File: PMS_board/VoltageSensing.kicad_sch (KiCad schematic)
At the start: 66 parts, among them J2 BAT_SENSE1, J3 BAT_SENSE2, U1 LM324DR, U2 LM324DR

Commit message: Voltage Sensing and Capacitor Assign
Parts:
- removed R7: 54.9k, Resistor_SMD:R_0603_1608Metric_Pad0.98x0.95mm_HandSolder, symbol Device:R_US
- removed TP1, TP4, TP5: TestPoint, TestPoint:TestPoint_Pad_D1.0mm, symbol Connector:TestPoint
- added D15, D22, D30, D31, D32, D33: BZV55B3V3, Diode_SMD:D_MiniMELF, symbol Diode:BZV55B3V3
- added R101, R102: 54.9k, Resistor_SMD:R_0603_1608Metric_Pad0.98x0.95mm_HandSolder, symbol Device:R_US
- added R103, R104, R105, R106, R107, R108, R109, R110, R111, R112, R113, R114: 39.2k, Resistor_SMD:R_0603_1608Metric_Pad0.98x0.95mm_HandSolder, symbol Device:R_US
- added R115, R116, R117, R118, R119, R120: 1k, Resistor_SMD:R_0603_1608Metric_Pad0.98x0.95mm_HandSolder, symbol Device:R_US
- added TP25, TP26, TP27: TestPoint, TestPoint:TestPoint_Pad_D1.0mm, symbol Connector:TestPoint
- added U15, U3: LM324DR, Package_SO:SOIC-14_3.9x8.7mm_P1.27mm, symbol Amplifier_Operational:Opamp_Quad
- added U19: TS3A27518EIPWRQ1, PW24, symbol Symbols:TS3A27518EIPWRQ1
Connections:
- net +24V: now also U15.4 (V+), U3.4 (V+)
- net BATT1_CELL1: now also R17.2, TP21.1
- net BATT1_CELL2: now also R15.2
- net BATT1_CELL3: now also R13.2
- net BATT1_CELL4: now also R11.2; no longer TP3.1
- net BATT1_CELL5: now also R9.2, TP3.1
- net BATT1_CELL6: now also TP20.1, R101.1
- net BATT2_CELL1: no longer R17.1, TP24.1
- net BATT2_CELL2: no longer R15.1, TP23.1
- net BATT2_CELL3: no longer R13.1, TP22.1
- net BATT2_CELL4: no longer R11.1, TP21.1
- net BATT2_CELL5: no longer R9.1, TP20.1
- net GND: now also D15.2 (A), D22.2 (A), D30.2 (A), D31.2 (A), D32.2 (A), D33.2 (A), R102.2, R103.1, R105.1, R107.1, R109.1, R111.1, R113.1, U15.11 (V-), U19.20 (*EN), U19.5 (GND), U3.11 (V-)
- net VSENSE1: now also U19.4 (COM1); no longer D8.1 (K), R36.2, TP12.1
- net VSENSE2: now also U19.6 (COM2); no longer D7.1 (K), R35.2, TP11.1
- net VSENSE3: now also U19.7 (COM3); no longer D6.1 (K), R34.2, TP10.1
- net VSENSE4: now also U19.9 (COM4); no longer D5.1 (K), R33.2, TP9.1
- net VSENSE5: now also U19.10 (COM5); no longer D4.1 (K), R31.2, TP8.1
- net VSENSE6: now also U19.12 (COM6); no longer D3.1 (K), R32.2, TP7.1
- net at R14.1, R26.1, R27.2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: no longer R15.2
- net at R10.1, R22.1, R23.2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: no longer R11.2
- net at R20.1, R21.2, R8.1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: no longer R9.2
- net at R12.1, R24.1, R25.2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: no longer R13.2
- net at R16.1, R28.1, R29.2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: no longer R17.2
- new net: R108.1, R109.2, R13.1, U15.13 (-), U3.10 (+)
- new net: R106.2, R115.1, U3.14
- new net: R112.2, R119.1, U15.1
- new net: R112.1, R113.2, R17.1, U15.2 (-), U3.5 (+)
- new net: R110.1, R111.2, R15.1, U15.3 (+), U3.9 (-)
- new net: R104.1, R105.2, R9.1, U3.12 (+), U3.2 (-)
- new net: R106.1, R107.2, R11.1, U15.12 (+), U3.13 (-)
- new net: R108.2, R117.1, U15.14
- new net: R110.2, R118.1, U3.8
- new net: R102.1, R114.1, U3.6 (-)
- new net: R114.2, R120.1, U3.7
- new net: R104.2, R116.1, U3.1
- new net: R101.2, R103.2, U3.3 (+)
- new net +3.3V: U19.8 (V+)
- new net BATT1_SENS1: D8.1 (K), R36.2, TP12.1, U19.2 (NC1)
- new net BATT1_SENS2: D7.1 (K), R35.2, TP11.1, U19.1 (NC2)
- new net BATT1_SENS3: D6.1 (K), R34.2, TP10.1, U19.23 (NC3)
- new net BATT1_SENS4: D5.1 (K), R33.2, TP9.1, U19.21 (NC4)
- new net BATT1_SENS5: D4.1 (K), R31.2, TP8.1, U19.19 (NC5)
- new net BATT1_SENS6: D3.1 (K), R32.2, TP7.1, U19.22 (NC6)
- new net BATT2_SENS1: D33.1 (K), R120.2, TP27.1, U19.11 (NO1)
- new net BATT2_SENS2: D32.1 (K), R119.2, TP26.1, U19.13 (NO2)
- new net BATT2_SENS3: D31.1 (K), R118.2, TP25.1, U19.15 (NO3)
- new net BATT2_SENS4: D30.1 (K), R117.2, TP24.1, U19.17 (NO4)
- new net BATT2_SENS5: D22.1 (K), R115.2, TP23.1, U19.18 (NO5)
- new net BATT2_SENS6: D15.1 (K), R116.2, TP22.1, U19.16 (NO6)
- new net SW1: U19.24 (IN1)
- new net SW2: U19.14 (IN2)
- no-connect marks 2 -> 3
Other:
- moved on the sheet: D3, D4, D5, D6, D7, D8, D9, J2, J3, R10, R100, R12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

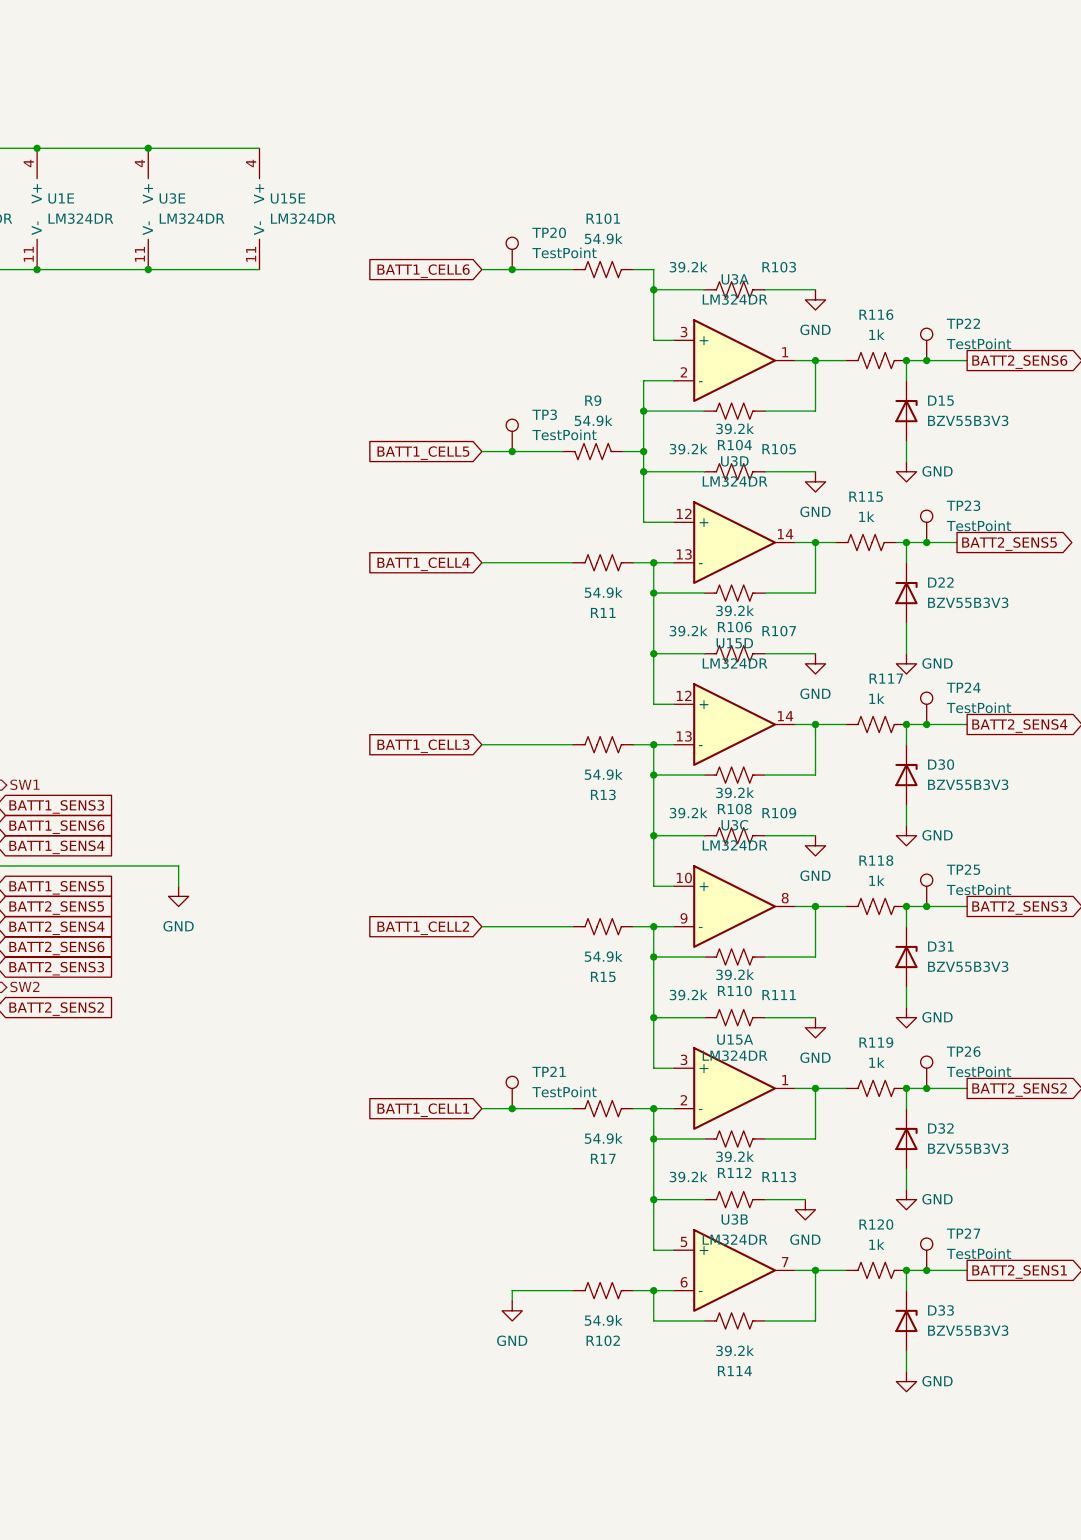
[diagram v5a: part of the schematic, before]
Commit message: Set some things to DNP
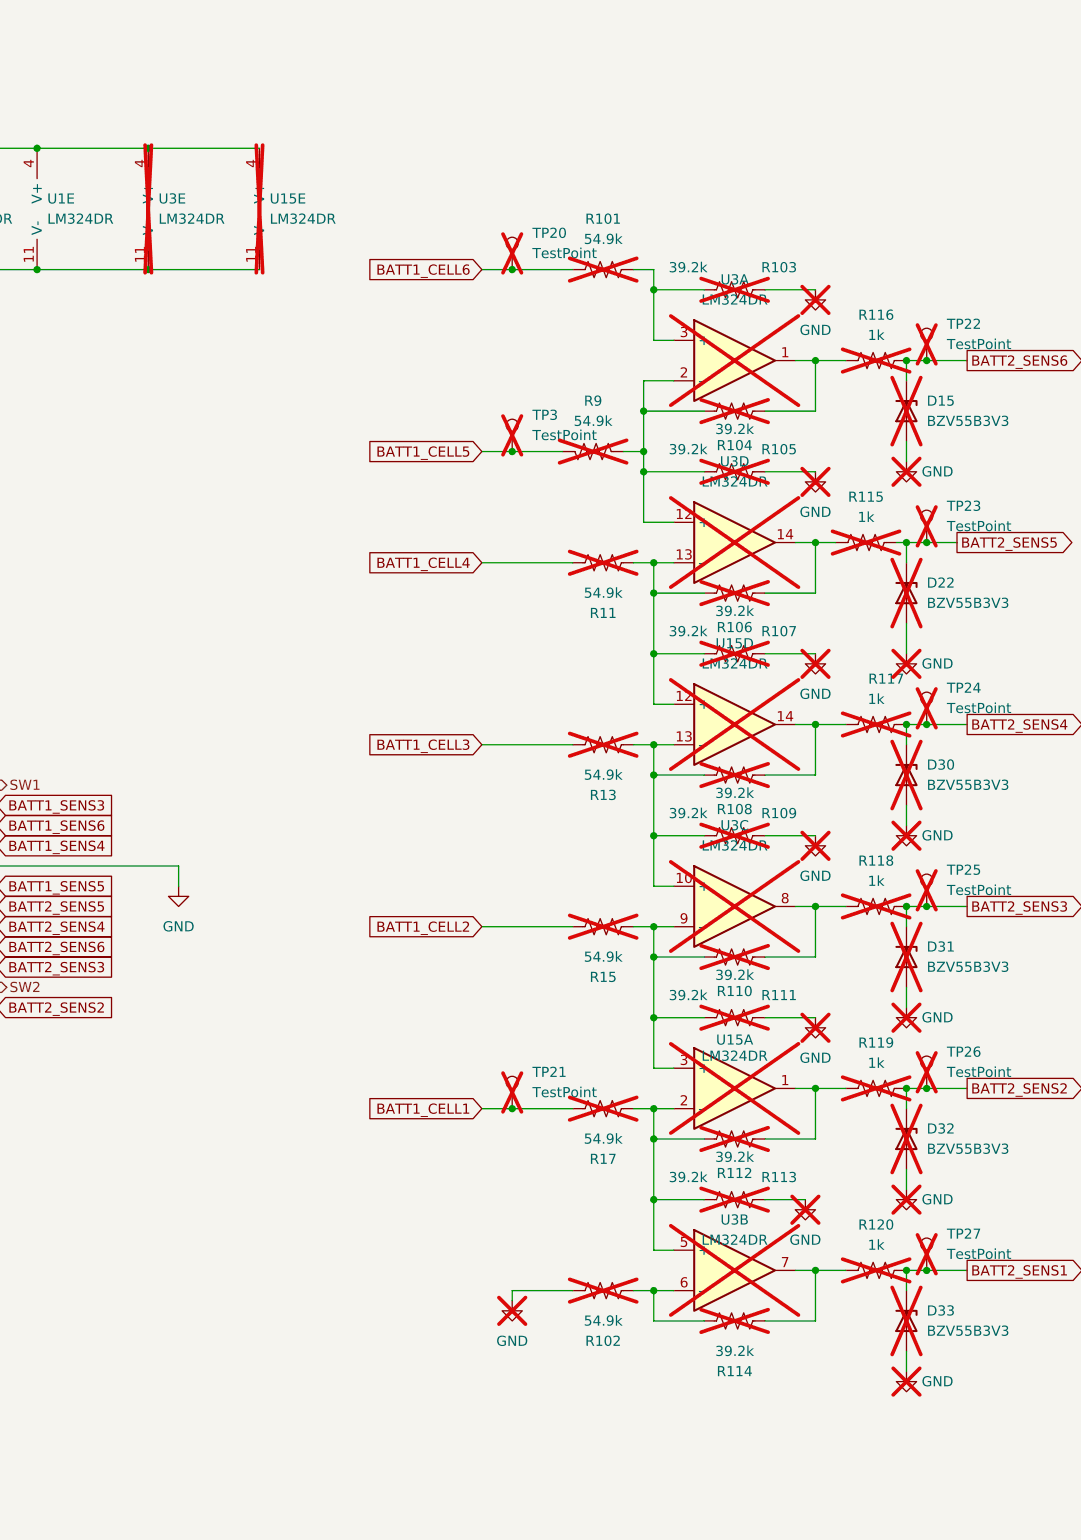
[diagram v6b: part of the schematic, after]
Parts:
- D15, D22, D30, D31, D32, D33, R101, R102, R103, R104, R105, R106, R107, R108, R109, R11, R110, R111, R112, R113, R114, R115, R116, R117, R118, R119, R120, R13, R15, R17, R9, TP20, TP21, TP22, TP23, TP24, TP25, TP26, TP27, TP3, U15, U3: now not fitted
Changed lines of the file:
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@@
 		(on_board yes)
 		(in_pos_files yes)
-		(dnp no)
+		(dnp yes)
 		(fields_autoplaced yes)
 		(property "Reference" "TP21"
@@
 		(on_board yes)
 		(in_pos_files yes)
-		(dnp no)
+		(dnp yes)
 		(fields_autoplaced yes)
 		(property "Reference" "D30"
@@
 		(on_board yes)
 		(in_pos_files yes)
-		(dnp no)
+		(dnp yes)
 		(fields_autoplaced yes)
 		(property "Reference" "#PWR0132"
@@
 		(on_board yes)
 		(in_pos_files yes)
-		(dnp no)
+		(dnp yes)
 		(fields_autoplaced yes)
 		(property "Reference" "TP26"
@@
 		(on_board yes)
 		(in_pos_files yes)
-		(dnp no)
+		(dnp yes)
 		(property "Reference" "R109"
 			(at 340.868 131.826 90)
@@
 		(on_board yes)
 		(in_pos_files yes)
-		(dnp no)
+		(dnp yes)
 		(fields_autoplaced yes)
 		(property "Reference" "R115"
@@
 		(on_board yes)
 		(in_pos_files yes)
-		(dnp no)
+		(dnp yes)
 		(property "Reference" "U15"
 			(at 335.28 160.274 0)
@@
 		(on_board yes)
 		(in_pos_files yes)
-		(dnp no)
+		(dnp yes)
 		(fields_autoplaced yes)
 		(property "Reference" "U3"
@@
 		(on_board yes)
 		(in_pos_files yes)
-		(dnp no)
+		(dnp yes)
 		(fields_autoplaced yes)
 		(property "Reference" "D33"
@@
 		(on_board yes)
 		(in_pos_files yes)
-		(dnp no)
+		(dnp yes)
 		(property "Reference" "R108"
 			(at 335.28 131.318 90)
@@
 		(on_board yes)
 		(in_pos_files yes)
-		(dnp no)
+		(dnp yes)
 		(fields_autoplaced yes)
 		(property "Reference" "#PWR0136"
@@
 		(on_board yes)
 		(in_pos_files yes)
-		(dnp no)
+		(dnp yes)
 		(fields_autoplaced yes)
 		(property "Reference" "#PWR0138"
@@
 		(on_board yes)
 		(in_pos_files yes)
-		(dnp no)
+		(dnp yes)
 		(fields_autoplaced yes)
 		(property "Reference" "#PWR075"
@@
 		(on_board yes)
 		(in_pos_files yes)
-		(dnp no)
+		(dnp yes)
 		(property "Reference" "R105"
 			(at 340.868 86.106 90)
@@
 		(on_board yes)
 		(in_pos_files yes)
-		(dnp no)
+		(dnp yes)
 		(fields_autoplaced yes)
 		(property "Reference" "U15"
@@
 		(on_board yes)
 		(in_pos_files yes)
-		(dnp no)
+		(dnp yes)
 		(fields_autoplaced yes)
 		(property "Reference" "R119"
@@
 		(on_board yes)
 		(in_pos_files yes)
-		(dnp no)
+		(dnp yes)
 		(fields_autoplaced yes)
 		(property "Reference" "U3"
@@
 		(on_board yes)
 		(in_pos_files yes)
-		(dnp no)
+		(dnp yes)
 		(property "Reference" "R111"
 			(at 340.868 154.686 90)
@@
 		(on_board yes)
 		(in_pos_files yes)
-		(dnp no)
+		(dnp yes)
 		(property "Reference" "R114"
 			(at 335.28 201.93 90)
@@
 		(on_board yes)
 		(in_pos_files yes)
-		(dnp no)
+		(dnp yes)
 		(fields_autoplaced yes)
 		(property "Reference" "TP20"
@@
 		(on_board yes)
 		(in_pos_files yes)
-		(dnp no)
+		(dnp yes)
 		(fields_autoplaced yes)
 		(property "Reference" "#PWR072"
@@
 		(on_board yes)
 		(in_pos_files yes)
-		(dnp no)
+		(dnp yes)
 		(property "Reference" "R9"
 			(at 317.5 80.01 90)
@@
 		(on_board yes)
 		(in_pos_files yes)
-		(dnp no)
+		(dnp yes)
 		(fields_autoplaced yes)
 		(property "Reference" "D15"
@@
 		(on_board yes)
 		(in_pos_files yes)
-		(dnp no)
+		(dnp yes)
 		(fields_autoplaced yes)
 		(property "Reference" "R118"
@@
 		(on_board yes)
 		(in_pos_files yes)
-		(dnp no)
+		(dnp yes)
 		(fields_autoplaced yes)
 		(property "Reference" "TP22"
@@
 		(on_board yes)
 		(in_pos_files yes)
-		(dnp no)
+		(dnp yes)
 		(fields_autoplaced yes)
 		(property "Reference" "TP25"
@@
 		(on_board yes)
 		(in_pos_files yes)
-		(dnp no)
+		(dnp yes)
 		(property "Reference" "R17"
 			(at 318.77 175.26 90)
@@
 		(on_board yes)
 		(in_pos_files yes)
-		(dnp no)
+		(dnp yes)
 		(property "Reference" "R102"
 			(at 318.77 198.12 90)
@@
 		(on_board yes)
 		(in_pos_files yes)
-		(dnp no)
+		(dnp yes)
 		(fields_autoplaced yes)
 		(property "Reference" "U15"
@@
 		(on_board yes)
 		(in_pos_files yes)
-		(dnp no)
+		(dnp yes)
 		(fields_autoplaced yes)
 		(property "Reference" "U3"
@@
 		(on_board yes)
 		(in_pos_files yes)
-		(dnp no)
+		(dnp yes)
 		(fields_autoplaced yes)
 		(property "Reference" "D32"
@@
 		(on_board yes)
 		(in_pos_files yes)
-		(dnp no)
+		(dnp yes)
 		(property "Reference" "R13"
 			(at 318.77 129.54 90)
@@
 		(on_board yes)
 		(in_pos_files yes)
-		(dnp no)
+		(dnp yes)
 		(fields_autoplaced yes)
 		(property "Reference" "D31"
@@
 		(on_board yes)
 		(in_pos_files yes)
-		(dnp no)
+		(dnp yes)
 		(property "Reference" "R113"
 			(at 340.868 177.546 90)
@@
 		(on_board yes)
 		(in_pos_files yes)
-		(dnp no)
+		(dnp yes)
 		(property "Reference" "R11"
 			(at 318.77 106.68 90)
@@
 		(on_board yes)
 		(in_pos_files yes)
-		(dnp no)
+		(dnp yes)
 		(property "Reference" "R112"
 			(at 335.28 177.038 90)
@@
 		(on_board yes)
 		(in_pos_files yes)
-		(dnp no)
+		(dnp yes)
 		(property "Reference" "R106"
 			(at 335.28 108.458 90)
@@
 		(on_board yes)
 		(in_pos_files yes)
-		(dnp no)
+		(dnp yes)
 		(fields_autoplaced yes)
 		(property "Reference" "#PWR030"
@@
 		(on_board yes)
 		(in_pos_files yes)
-		(dnp no)
+		(dnp yes)
 		(fields_autoplaced yes)
 		(property "Reference" "D22"
@@
 		(on_board yes)
 		(in_pos_files yes)
-		(dnp no)
+		(dnp yes)
 		(property "Reference" "R103"
 			(at 340.868 63.246 90)
@@
 		(on_board yes)
 		(in_pos_files yes)
-		(dnp no)
+		(dnp yes)
 		(fields_autoplaced yes)
 		(property "Reference" "#PWR071"
@@
 		(on_board yes)
 		(in_pos_files yes)
-		(dnp no)
+		(dnp yes)
 		(fields_autoplaced yes)
 		(property "Reference" "#PWR026"
@@
 		(on_board yes)
 		(in_pos_files yes)
-		(dnp no)
+		(dnp yes)
 		(property "Reference" "R101"
 			(at 318.77 57.15 90)
@@
 		(on_board yes)
 		(in_pos_files yes)
-		(dnp no)
+		(dnp yes)
 		(fields_autoplaced yes)
 		(property "Reference" "#PWR0135"
@@
 		(on_board yes)
 		(in_pos_files yes)
-		(dnp no)
+		(dnp yes)
 		(fields_autoplaced yes)
 		(property "Reference" "U3"
@@
 		(on_board yes)
 		(in_pos_files yes)
-		(dnp no)
+		(dnp yes)
 		(property "Reference" "R107"
 			(at 340.868 108.966 90)
@@
 		(on_board yes)
 		(in_pos_files yes)
-		(dnp no)
+		(dnp yes)
 		(property "Reference" "R110"
 			(at 335.28 154.178 90)
@@
 		(on_board yes)
 		(in_pos_files yes)
-		(dnp no)
+		(dnp yes)
 		(fields_autoplaced yes)
 		(property "Reference" "#PWR027"
@@
 		(on_board yes)
 		(in_pos_files yes)
-		(dnp no)
+		(dnp yes)
 		(fields_autoplaced yes)
 		(property "Reference" "R116"
@@
 		(on_board yes)
 		(in_pos_files yes)
-		(dnp no)
+		(dnp yes)
 		(fields_autoplaced yes)
 		(property "Reference" "TP3"
@@
 		(on_board yes)
 		(in_pos_files yes)
-		(dnp no)
+		(dnp yes)
 		(property "Reference" "R15"
 			(at 318.77 152.4 90)
@@
 		(on_board yes)
 		(in_pos_files yes)
-		(dnp no)
+		(dnp yes)
 		(fields_autoplaced yes)
 		(property "Reference" "TP24"
@@
 		(on_board yes)
 		(in_pos_files yes)
-		(dnp no)
+		(dnp yes)
 		(fields_autoplaced yes)
 		(property "Reference" "#PWR0137"
@@
 		(on_board yes)
 		(in_pos_files yes)
-		(dnp no)
+		(dnp yes)
 		(property "Reference" "R117"
 			(at 354.33 114.935 90)
@@
 		(on_board yes)
 		(in_pos_files yes)
-		(dnp no)
+		(dnp yes)
 		(fields_autoplaced yes)
 		(property "Reference" "TP27"
@@
 		(on_board yes)
 		(in_pos_files yes)
-		(dnp no)
+		(dnp yes)
 		(property "Reference" "U3"
 			(at 335.28 182.88 0)
@@
 		(on_board yes)
 		(in_pos_files yes)
-		(dnp no)
+		(dnp yes)
 		(property "Reference" "R104"
 			(at 335.28 85.598 90)
@@
 		(on_board yes)
 		(in_pos_files yes)
-		(dnp no)
+		(dnp yes)
 		(fields_autoplaced yes)
 		(property "Reference" "#PWR0134"
@@
 		(on_board yes)
 		(in_pos_files yes)
-		(dnp no)
+		(dnp yes)
 		(fields_autoplaced yes)
 		(property "Reference" "TP23"
@@
 		(on_board yes)
 		(in_pos_files yes)
-		(dnp no)
+		(dnp yes)
 		(fields_autoplaced yes)
 		(property "Reference" "#PWR0133"
@@
 		(on_board yes)
 		(in_pos_files yes)
-		(dnp no)
+		(dnp yes)
 		(fields_autoplaced yes)
 		(property "Reference" "R120"

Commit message: Uh oh merge conflicts
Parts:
- removed D15, D22, D30, D31, D32, D33: BZV55B3V3, Diode_SMD:D_MiniMELF, symbol Diode:BZV55B3V3
- removed R101, R102, R11, R13, R15, R17, R9: 54.9k, Resistor_SMD:R_0603_1608Metric_Pad0.98x0.95mm_HandSolder, symbol Device:R_US
- removed R103, R104, R105, R106, R107, R108, R109, R110, R111, R112, R113, R114: 39.2k, Resistor_SMD:R_0603_1608Metric_Pad0.98x0.95mm_HandSolder, symbol Device:R_US
- removed R115, R116, R117, R118, R119, R120: 1k, Resistor_SMD:R_0603_1608Metric_Pad0.98x0.95mm_HandSolder, symbol Device:R_US
- removed TP19, TP2, TP20, TP21, TP22, TP23, TP24, TP25, TP26, TP27, TP3, TP6: TestPoint, TestPoint:TestPoint_Pad_D1.0mm, symbol Connector:TestPoint
- removed U15, U3: LM324DR, Package_SO:SOIC-14_3.9x8.7mm_P1.27mm, symbol Amplifier_Operational:Opamp_Quad
- U19: footprint PW24 -> TS3A27518RIPWRQ1:PW24
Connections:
- net BATT2_SENS1 is gone; now on net BATT2_CELL1: U19.11 (NO1)
- net BATT2_SENS2 is gone; now on net BATT2_CELL2: U19.13 (NO2)
- net BATT2_SENS3 is gone; now on net BATT2_CELL3: U19.15 (NO3)
- net BATT2_SENS4 is gone; now on net BATT2_CELL4: U19.17 (NO4)
- net BATT2_SENS5 is gone; now on net BATT2_CELL5: U19.18 (NO5)
- net BATT2_SENS6 is gone; now on net BATT2_CELL6: U19.16 (NO6)
- net SW2 is gone; now on net CELL_SW: U19.14 (IN2)
- net BATT1_CELL1: now also U19.2 (NC1); no longer R16.2
- net BATT1_CELL2: now also U19.1 (NC2); no longer R14.2
- net BATT1_CELL3: now also U19.23 (NC3); no longer R12.2
- net BATT1_CELL4: now also U19.21 (NC4); no longer R10.2
- net BATT1_CELL5: now also U19.19 (NC5); no longer R8.2
- net BATT1_CELL6: now also U19.22 (NC6); no longer R100.1
- net VSENSE1: now also D8.1 (K), R36.2, TP12.1; no longer U19.4 (COM1)
- net VSENSE2: now also D7.1 (K), R35.2, TP11.1; no longer U19.6 (COM2)
- net VSENSE3: now also D6.1 (K), R34.2, TP10.1; no longer U19.7 (COM3)
- net VSENSE4: now also D5.1 (K), R33.2, TP9.1; no longer U19.9 (COM4)
- net VSENSE5: now also D4.1 (K), R31.2, TP8.1; no longer U19.10 (COM5)
- net VSENSE6: now also D3.1 (K), R32.2, TP7.1; no longer U19.12 (COM6)
- removed net BATT1_SENS1: D8.1 (K), R36.2, TP12.1, U19.2 (NC1)
- removed net BATT1_SENS2: D7.1 (K), R35.2, TP11.1, U19.1 (NC2)
- removed net BATT1_SENS3: D6.1 (K), R34.2, TP10.1, U19.23 (NC3)
- removed net BATT1_SENS4: D5.1 (K), R33.2, TP9.1, U19.21 (NC4)
- removed net BATT1_SENS5: D4.1 (K), R31.2, TP8.1, U19.19 (NC5)
- removed net BATT1_SENS6: D3.1 (K), R32.2, TP7.1, U19.22 (NC6)
- net SW1 renamed CELL_SW
- new net COM_CELL1: R16.2, U19.4 (COM1)
- new net COM_CELL2: R14.2, U19.6 (COM2)
- new net COM_CELL3: R12.2, U19.7 (COM3)
- new net COM_CELL4: R10.2, U19.9 (COM4)
- new net COM_CELL5: R8.2, U19.10 (COM5)
- new net COM_CELL6: R100.1, U19.12 (COM6)
